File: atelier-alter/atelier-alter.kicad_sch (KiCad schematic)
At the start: 28 parts, among them SW1 SW_Push, U1 ATmega32U4-A, Y1 16Mhz

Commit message: redrawn
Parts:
- added C10, C11, C8, C9: 100nF, Capacitor_SMD:C_0805_2012Metric, symbol Device:C_Small
- added D10, D7, D8, D9: SK6812, LED_SMD:LED_SK6812_PLCC4_5.0x5.0mm_P3.2mm, symbol LED:SK6812
- added R5: 300, Resistor_SMD:R_0805_2012Metric, symbol Device:R_Small
- C2: value C_Small -> 1uF
- C7: value 0.1uF -> 10uF
- R1, R2: value R_Small -> 22
- SW1: value SW_Push -> RESET
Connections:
- net +5V: now also C10.1, C11.1, C8.1, C9.1, D10.3 (VDD), D7.3 (VDD), D8.3 (VDD), D9.3 (VDD)
- net COL1: now also U1.11 (PB3)
- net COL2: now also U1.28 (PB4)
- net COL3: now also U1.29 (PB5)
- net GND: now also C10.2, C11.2, C8.2, C9.2, D10.1 (VSS), D7.1 (VSS), D8.1 (VSS), D9.1 (VSS)
- net ROW1: now also U1.27 (PD7)
- net ROW2: now also U1.30 (PB6)
- net UGLOW1: now reaches U1.41 (PF0)
- net UGLOW1: now also R5.1
- new net: D10.2 (DIN), D9.4 (DOUT)
- new net: D7.4 (DOUT), D8.2 (DIN)
- new net: D8.4 (DOUT), D9.2 (DIN)
- new net: D7.2 (DIN), R5.2
- no-connect marks 0 -> 23
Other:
- moved on the sheet: D1, D2, D3, D4, D5, D6, MX1, MX2, MX3, MX4, MX5, MX6

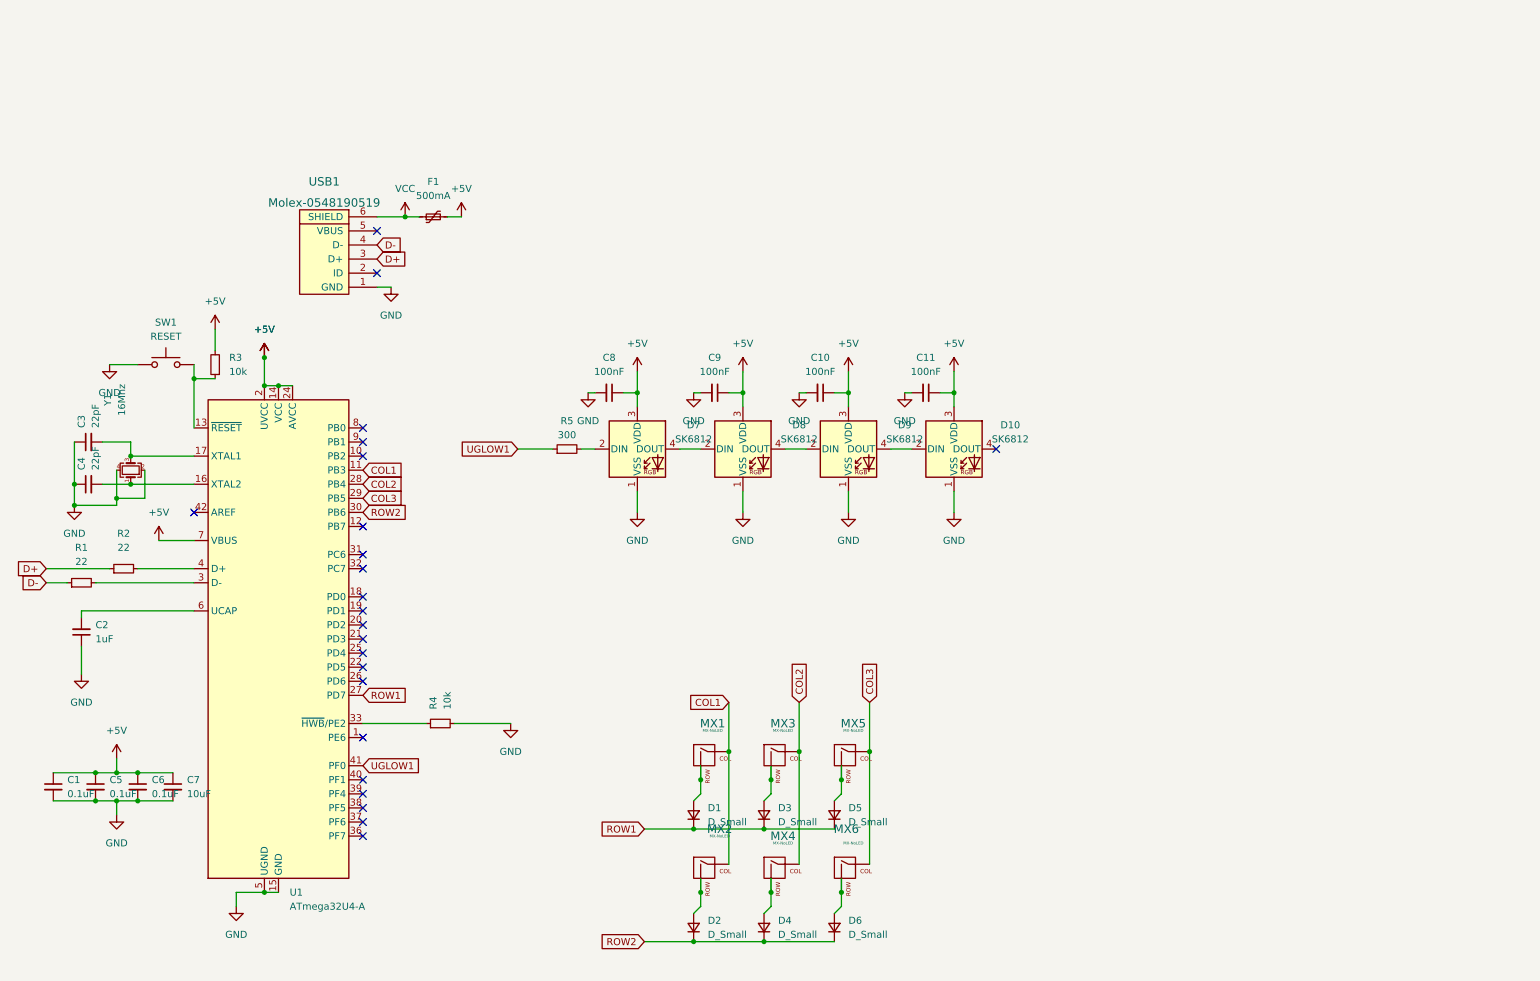
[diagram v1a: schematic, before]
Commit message: redrawn lan 3, them vai chuc nang
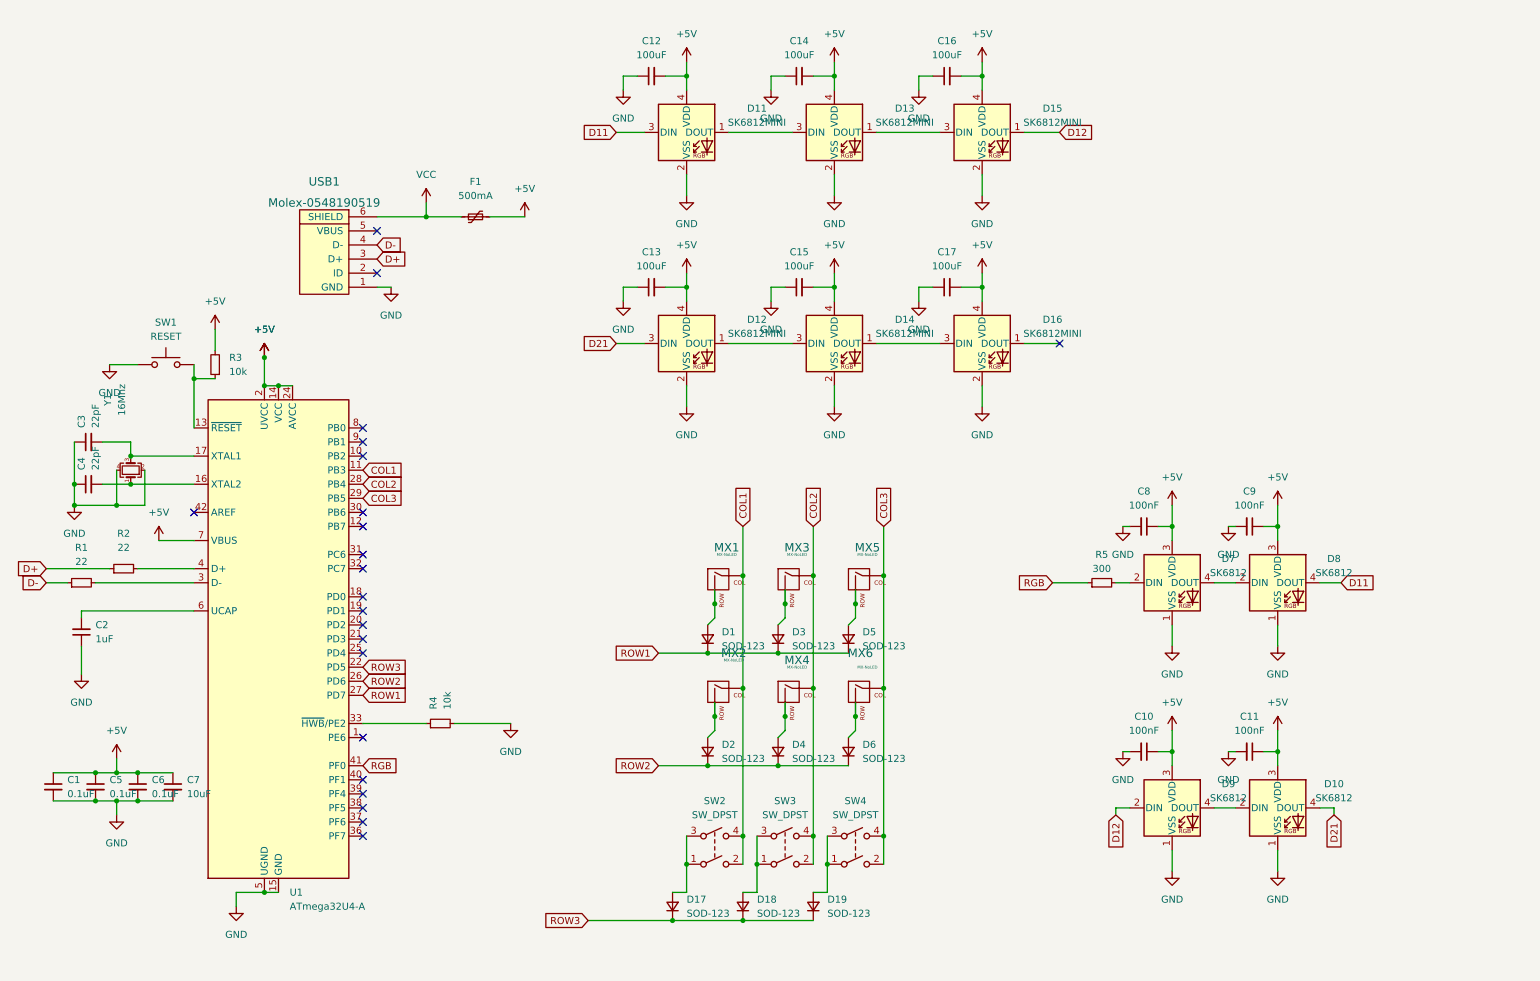
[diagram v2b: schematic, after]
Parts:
- added C12, C13, C14, C15, C16, C17: 100uF, Capacitor_SMD:C_0805_2012Metric, symbol Device:C_Small
- added D11, D12, D13, D14, D15, D16: SK6812MINI, LED_SMD:LED_SK6812MINI_PLCC4_3.5x3.5mm_P1.75mm, symbol LED:SK6812MINI
- added D17, D18, D19: SOD-123, Diode_SMD:D_SOD-123, symbol Device:D_Small
- added SW2, SW3, SW4: SW_DPST, Button_Switch_THT:SW_PUSH_6mm_H9.5mm, symbol Switch:SW_DPST
- D1, D2, D3, D4, D5, D6: value D_Small -> SOD-123
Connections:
- net +5V: now also C12.2, C13.2, C14.2, C15.2, C16.2, C17.2, D11.4 (VDD), D12.4 (VDD), D13.4 (VDD), D14.4 (VDD), D15.4 (VDD), D16.4 (VDD)
- net COL1: now also SW2.2, SW2.4
- net COL2: now also SW3.2, SW3.4
- net COL3: now also SW4.2, SW4.4
- net GND: now also C12.1, C13.1, C14.1, C15.1, C16.1, C17.1, D11.2 (VSS), D12.2 (VSS), D13.2 (VSS), D14.2 (VSS), D15.2 (VSS), D16.2 (VSS)
- net ROW2: now also U1.26 (PD6); no longer U1.30 (PB6)
- net D21: now reaches D10.4 (DOUT)
- net D21: now also D12.3 (DIN)
- net D11: now reaches D8.4 (DOUT)
- net D11: now also D11.3 (DIN); no longer D9.2 (DIN)
- net ROW3: now reaches U1.22 (PD5)
- net ROW3: now also D17.1 (K), D18.1 (K), D19.1 (K)
- net UGLOW1 renamed RGB
- new net: D13.1 (DOUT), D15.3 (DIN)
- new net: D19.2 (A), SW4.1, SW4.3
- new net: D11.1 (DOUT), D13.3 (DIN)
- new net: D18.2 (A), SW3.1, SW3.3
- new net: D12.1 (DOUT), D14.3 (DIN)
- new net: D17.2 (A), SW2.1, SW2.3
- new net: D14.1 (DOUT), D16.3 (DIN)
- new net D12: D15.1 (DOUT), D9.2 (DIN)
- no-connect marks 23 -> 22
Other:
- moved on the sheet: C10, C11, C8, C9, D1, D10, D2, D3, D4, D5, D6, D7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

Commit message: add essentials
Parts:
- removed F1: 500mA, Fuse:Fuse_1206_3216Metric, symbol Device:Polyfuse_Small
- removed USB1: Molex-0548190519, random-keyboard-parts:Molex-0548190589, symbol random-keyboard-parts:Molex-0548190519
- added R6, R7: 5.1k, Capacitor_SMD:C_0805_2012Metric, symbol Device:R_Small
- added U2: PRTR5V0U2X, Package_TO_SOT_SMD:SOT-143_Handsoldering, symbol random-keyboard-parts:PRTR5V0U2X
- added USB1: HRO-TYPE-C-31-M-12, Type-C:HRO-TYPE-C-31-M-12-HandSoldering, symbol Satxri6key-rescue:HRO-TYPE-C-31-M-12-Type-C-random-keyboard-parts
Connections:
- net +5V: now also U2.4 (VCC), USB1.11 (VBUS), USB1.2 (VBUS)
- net COL1: now also U1.19 (PD1); no longer U1.11 (PB3)
- net COL2: now also U1.20 (PD2); no longer U1.28 (PB4)
- net COL3: now also U1.21 (PD3); no longer U1.29 (PB5)
- net D+: now also U2.2 (IO1), USB1.6 (DP1), USB1.8 (DP2)
- net D-: now also U2.3 (IO2), USB1.5 (DN2), USB1.7 (DN1)
- net GND: now also R6.1, R7.1, U2.1 (GND), USB1.1 (GND), USB1.12 (GND), USB1.13 (SHIELD)
- net RGB: now also U1.18 (PD0); no longer U1.41 (PF0)
- new net: R7.2, USB1.10 (CC2)
- new net: R6.2, USB1.4 (CC1)
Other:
- moved on the sheet: C10, C11, C8, C9, D10, D7, D8, D9, R5

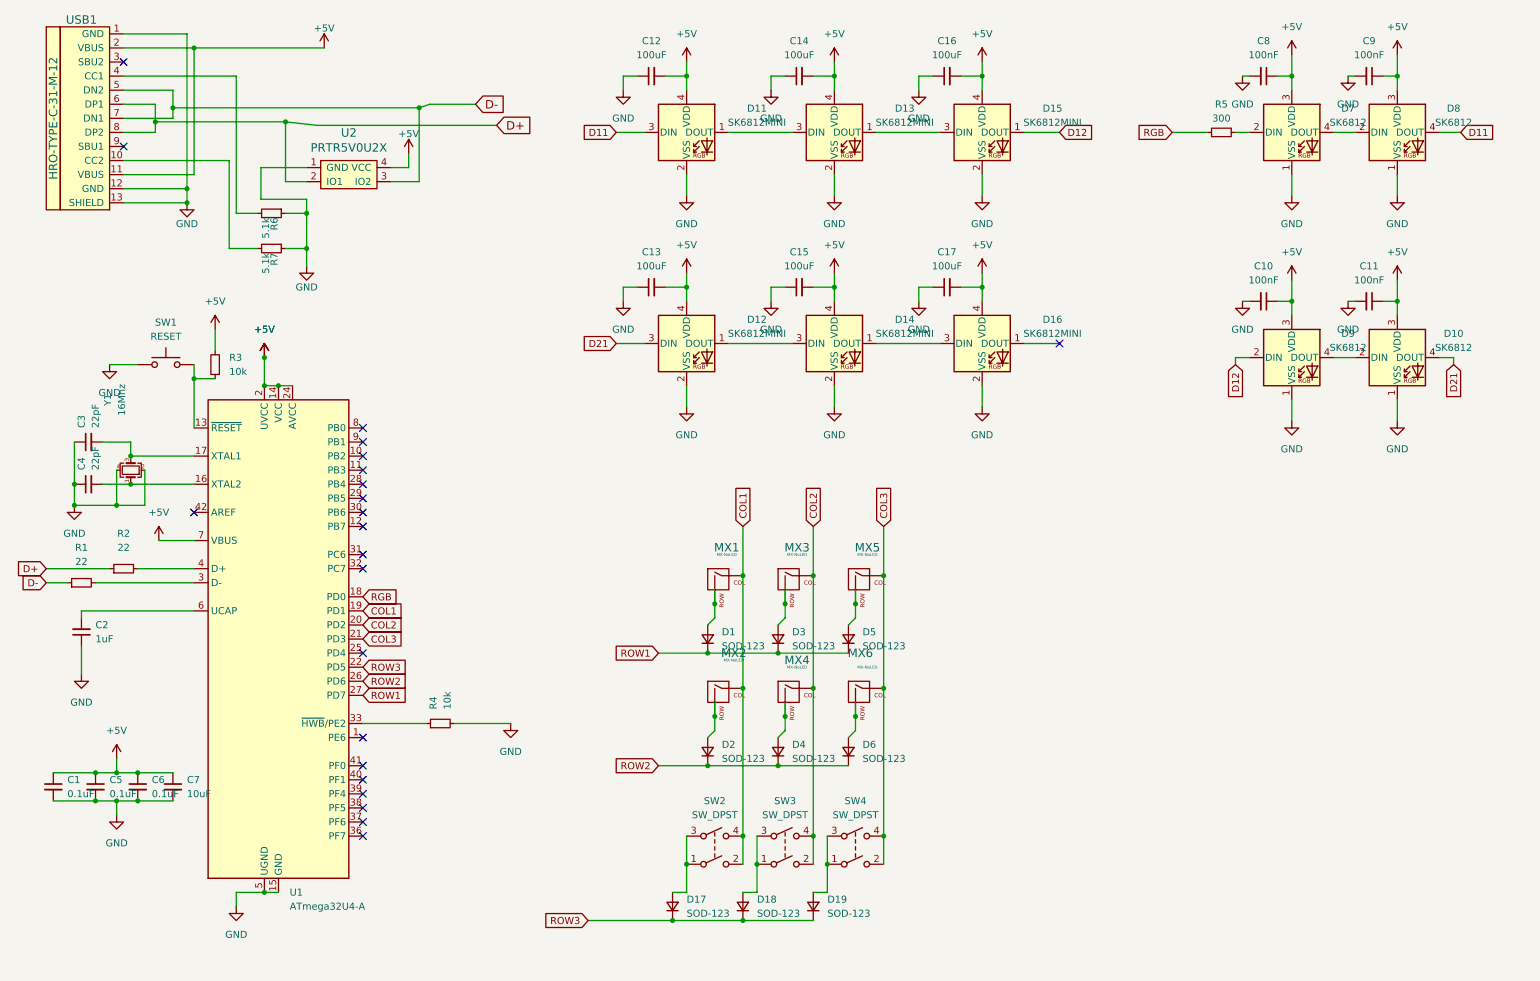
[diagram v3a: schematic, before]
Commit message: update footprint, route lai mach, giam manh so luong vias
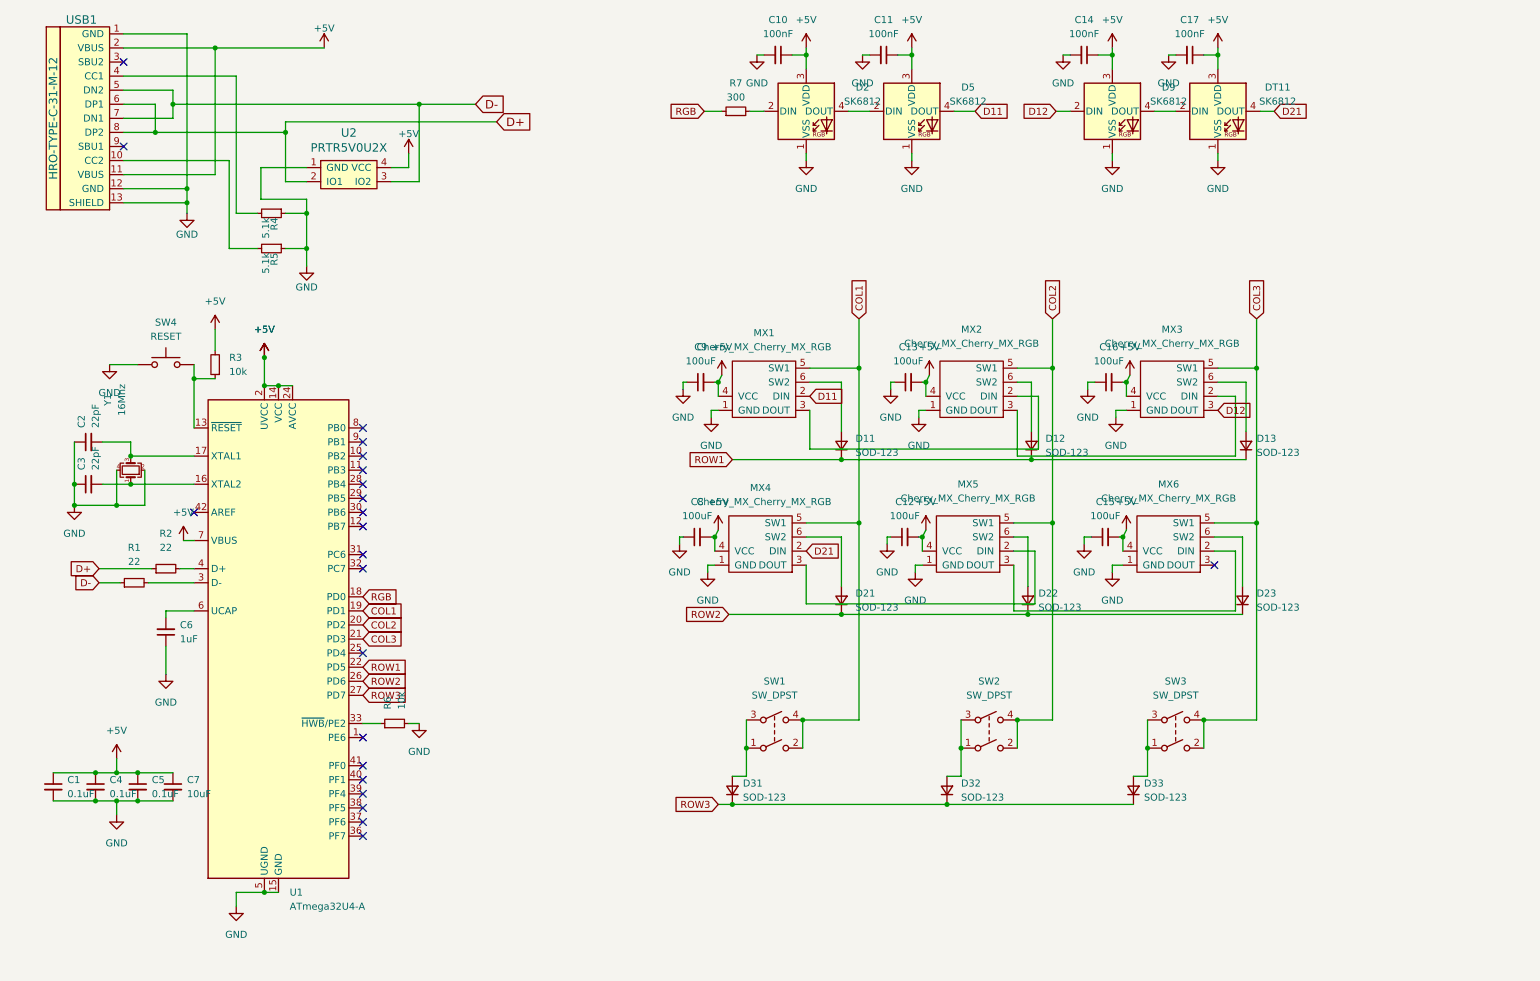
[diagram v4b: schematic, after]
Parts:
- removed C14, C17: 100uF, Capacitor_SMD:C_0805_2012Metric, symbol Device:C_Small
- removed D1, D2, D3, D4, D5, D6: SOD-123, Diode_SMD:D_SOD-123, symbol Device:D_Small
- removed D11, D12, D13, D14, D15, D16: SK6812MINI, LED_SMD:LED_SK6812MINI_PLCC4_3.5x3.5mm_P1.75mm, symbol LED:SK6812MINI
- removed MX1, MX2, MX3, MX4, MX5, MX6: MX-NoLED, MX_Only:MXOnly-1U-Hotswap, symbol MX_Alps_Hybrid:MX-NoLED
- added C8, C9: 100uF, Capacitor_SMD:C_0805_2012Metric, symbol Device:C_Small
- added D11, D12, D13, D21, D22, D23: SOD-123, Diode_SMD:D_SOD-123, symbol Device:D_Small
- added MX1, MX2, MX3, MX4, MX5, MX6: Cherry_MX_Cherry_MX_RGB, Cherry MX:Cherry-MX_PCB-Mounted_LTST-A683CEGBW_Kailh_Socket, symbol Cherry MX Breakout Board (Kailh Socket)-cache:Cherry_MX_Cherry_MX_RGB
- renumbered C8 to C10, C9 to C11, C10 to C14, C11 to C17, C3 to C2, C4 to C3, C5 to C4, C6 to C5, C2 to C6, D7 to D2, D17 to D31, D18 to D32, D19 to D33, D8 to D5, D10 to DT11, R6 to R4, R7 to R5, R4 to R6, R5 to R7, SW2 to SW1, SW3 to SW2, SW4 to SW3, SW1 to SW4
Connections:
- net +5V: now also C8.2, C9.2, MX1.4 (VCC), MX2.4 (VCC), MX3.4 (VCC), MX4.4 (VCC), MX5.4 (VCC), MX6.4 (VCC)
- net COL1: now also MX1.5 (SW1), MX4.5 (SW1)
- net COL2: now also MX2.5 (SW1), MX5.5 (SW1)
- net COL3: now also MX3.5 (SW1), MX6.5 (SW1)
- net D11: now also MX1.2 (DIN)
- net D12: now also MX3.3 (DOUT)
- net D21: now also MX4.2 (DIN)
- net GND: now also C8.1, C9.1, MX1.1 (GND), MX2.1 (GND), MX3.1 (GND), MX4.1 (GND), MX5.1 (GND), MX6.1 (GND)
- net ROW1: now also U1.22 (PD5), D11.1 (K), D12.1 (K), D13.1 (K); no longer U1.27 (PD7)
- net ROW2: now also D21.1 (K), D22.1 (K), D23.1 (K)
- net ROW3: now also U1.27 (PD7); no longer U1.22 (PD5)
- new net: D22.2 (A), MX5.6 (SW2)
- new net: MX4.3 (DOUT), MX5.2 (DIN)
- new net: MX5.3 (DOUT), MX6.2 (DIN)
- new net: MX1.3 (DOUT), MX2.2 (DIN)
- new net: MX2.3 (DOUT), MX3.2 (DIN)
- new net: D12.2 (A), MX2.6 (SW2)
- new net: D21.2 (A), MX4.6 (SW2)
- new net: D13.2 (A), MX3.6 (SW2)
- new net: D11.2 (A), MX1.6 (SW2)
- new net: D23.2 (A), MX6.6 (SW2)
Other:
- moved on the sheet: C10, C11, C14, C17, C6, D2, D31, D32, D33, D5, D9, DT11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

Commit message: add M2 mounting hole
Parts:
- added H1, H2, H3, H4: MountingHole, MountingHole:MountingHole_2.5mm, symbol Mechanical:MountingHole
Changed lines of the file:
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@@
     (pin "2")
+  )
+  (symbol (lib_id "Mechanical:MountingHole") (at 129.54 186.69 0) (unit 1)
+    (in_bom yes) (on_board yes) (fields_autoplaced)
+    (property "Reference" "H4" (id 0) (at 132.08 185.4199 0)
+      (effects (font (size 1.27 1.27)) (justify left))
+    )
+    (property "Value" "MountingHole" (id 1) (at 132.08 187.9599 0)
+      (effects (font (size 1.27 1.27)) (justify left))
+    )
+    (property "Footprint" "MountingHole:MountingHole_2.5mm" (id 2) (at 129.54 186.69 0)
+      (effects (font (size 1.27 1.27)) hide)
+    )
+    (property "Datasheet" "~" (id 3) (at 129.54 186.69 0)
+      (effects (font (size 1.27 1.27)) hide)
+    )
   )
   (symbol (lib_id "power:GND") (at 175.26 89.535 0) (unit 1)
@@
     (pin "2")
   )
+  (symbol (lib_id "Mechanical:MountingHole") (at 106.68 186.69 0) (unit 1)
+    (in_bom yes) (on_board yes) (fields_autoplaced)
+    (property "Reference" "H2" (id 0) (at 109.22 185.4199 0)
+      (effects (font (size 1.27 1.27)) (justify left))
+    )
+    (property "Value" "MountingHole" (id 1) (at 109.22 187.9599 0)
+      (effects (font (size 1.27 1.27)) (justify left))
+    )
+    (property "Footprint" "MountingHole:MountingHole_2.5mm" (id 2) (at 106.68 186.69 0)
+      (effects (font (size 1.27 1.27)) hide)
+    )
+    (property "Datasheet" "~" (id 3) (at 106.68 186.69 0)
+      (effects (font (size 1.27 1.27)) hide)
+    )
+  )
   (symbol (lib_id "Device:C_Small") (at 224.155 24.13 270) (unit 1)
     (in_bom yes) (on_board yes) (fields_autoplaced)
@@
     (pin "1")
     (pin "2")
+  )
+  (symbol (lib_id "Mechanical:MountingHole") (at 106.68 176.53 0) (unit 1)
+    (in_bom yes) (on_board yes) (fields_autoplaced)
+    (property "Reference" "H1" (id 0) (at 109.22 175.2599 0)
+      (effects (font (size 1.27 1.27)) (justify left))
+    )
+    (property "Value" "MountingHole" (id 1) (at 109.22 177.7999 0)
+      (effects (font (size 1.27 1.27)) (justify left))
+    )
+    (property "Footprint" "MountingHole:MountingHole_2.5mm" (id 2) (at 106.68 176.53 0)
+      (effects (font (size 1.27 1.27)) hide)
+    )
+    (property "Datasheet" "~" (id 3) (at 106.68 176.53 0)
+      (effects (font (size 1.27 1.27)) hide)
+    )
   )
   (symbol (lib_id "power:GND") (at 39.37 135.89 0) (unit 1)
@@
     (pin "2")
   )
+  (symbol (lib_id "Mechanical:MountingHole") (at 129.54 176.53 0) (unit 1)
+    (in_bom yes) (on_board yes) (fields_autoplaced)
+    (property "Reference" "H3" (id 0) (at 132.08 175.2599 0)
+      (effects (font (size 1.27 1.27)) (justify left))
+    )
+    (property "Value" "MountingHole" (id 1) (at 132.08 177.7999 0)
+      (effects (font (size 1.27 1.27)) (justify left))
+    )
+    (property "Footprint" "MountingHole:MountingHole_2.5mm" (id 2) (at 129.54 176.53 0)
+      (effects (font (size 1.27 1.27)) hide)
+    )
+    (property "Datasheet" "~" (id 3) (at 129.54 176.53 0)
+      (effects (font (size 1.27 1.27)) hide)
+    )
+  )
   (symbol (lib_id "power:GND") (at 169.545 112.395 0) (unit 1)
     (in_bom yes) (on_board yes) (fields_autoplaced)
@@
       (reference "DT11") (unit 1) (value "SK6812") (footprint "LED_SMD:LED_SK6812_PLCC4_5.0x5.0mm_P3.2mm")
     )
+    (path "/8556b1bc-59f1-44d9-99ff-e1f2c0ffcf36"
+      (reference "H1") (unit 1) (value "MountingHole") (footprint "MountingHole:MountingHole_2.5mm")
+    )
+    (path "/5a99e80a-11b8-48d3-b554-660c0bcf5c38"
+      (reference "H2") (unit 1) (value "MountingHole") (footprint "MountingHole:MountingHole_2.5mm")
+    )
+    (path "/9a99f614-4356-46fa-a338-e647cb700704"
+      (reference "H3") (unit 1) (value "MountingHole") (footprint "MountingHole:MountingHole_2.5mm")
+    )
+    (path "/3b67de7c-1c99-408a-a31c-508b13725aa4"
+      (reference "H4") (unit 1) (value "MountingHole") (footprint "MountingHole:MountingHole_2.5mm")
+    )
     (path "/92fbf038-747f-4dcc-ac4a-6dcc9e81a6d6"

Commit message: rework mot chut
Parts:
- C12, C13, C15, C16, C8, C9: value 100uF -> 100nF
- R4, R5: footprint Capacitor_SMD:C_0805_2012Metric -> Resistor_SMD:R_0805_2012Metric
- renumbered DT11 to D14
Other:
- moved on the sheet: D11, D12, D21, D22
